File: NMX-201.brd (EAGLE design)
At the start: 50.8 x 50.2 mm, 61 parts, among them IC1 A4983TOP, IC2 A4983TOP, IC3 A4983TOP, J1 MOLEX-4-RA, J2 MOLEX-4-RA, J3 MOLEX-4-RA, U1 CADJ, U2 CADJ, U3 MOUNT-HOLE3.2, U4 MOUNT-HOLE3.2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

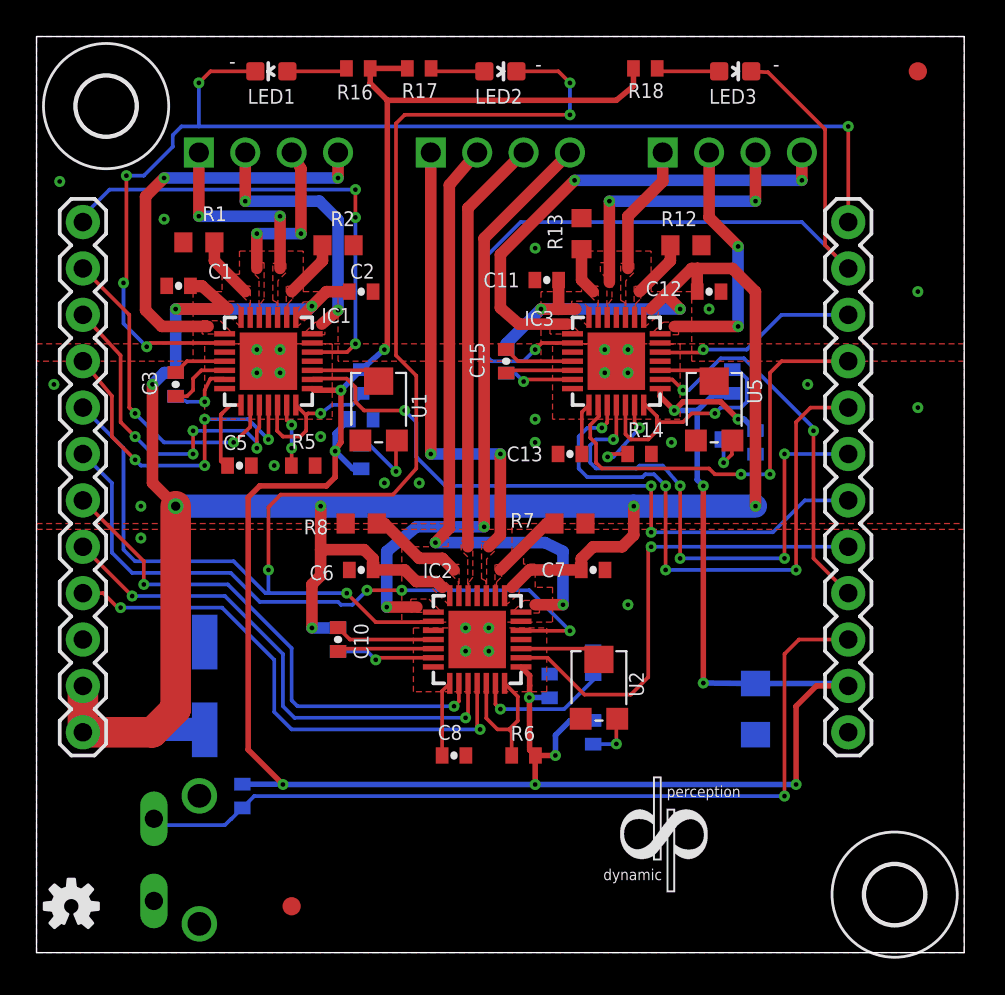
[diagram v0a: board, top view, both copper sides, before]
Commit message: Update to Silk Screen
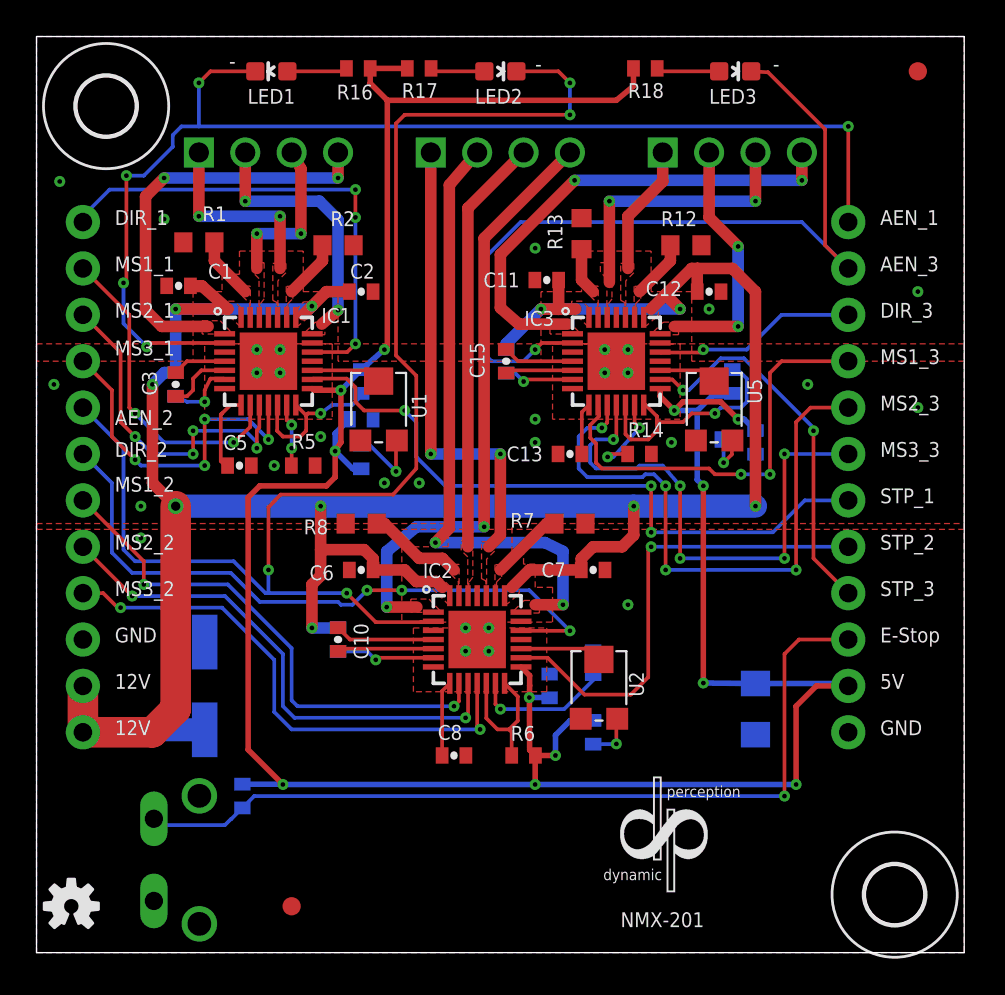
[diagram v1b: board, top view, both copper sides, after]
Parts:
- flipped JP3 to the bottom
- flipped JP4 to the bottom

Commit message: Updated NMX-201 to match NMX-201B
The only difference between NMX-201 and NMX-201B is whether the the
component attached to the motor connector ports is a screw terminal or a
Molex connector, so there's really no need to maintain two different
schematics / board files. These differences should be reflected in the
BOM instead.
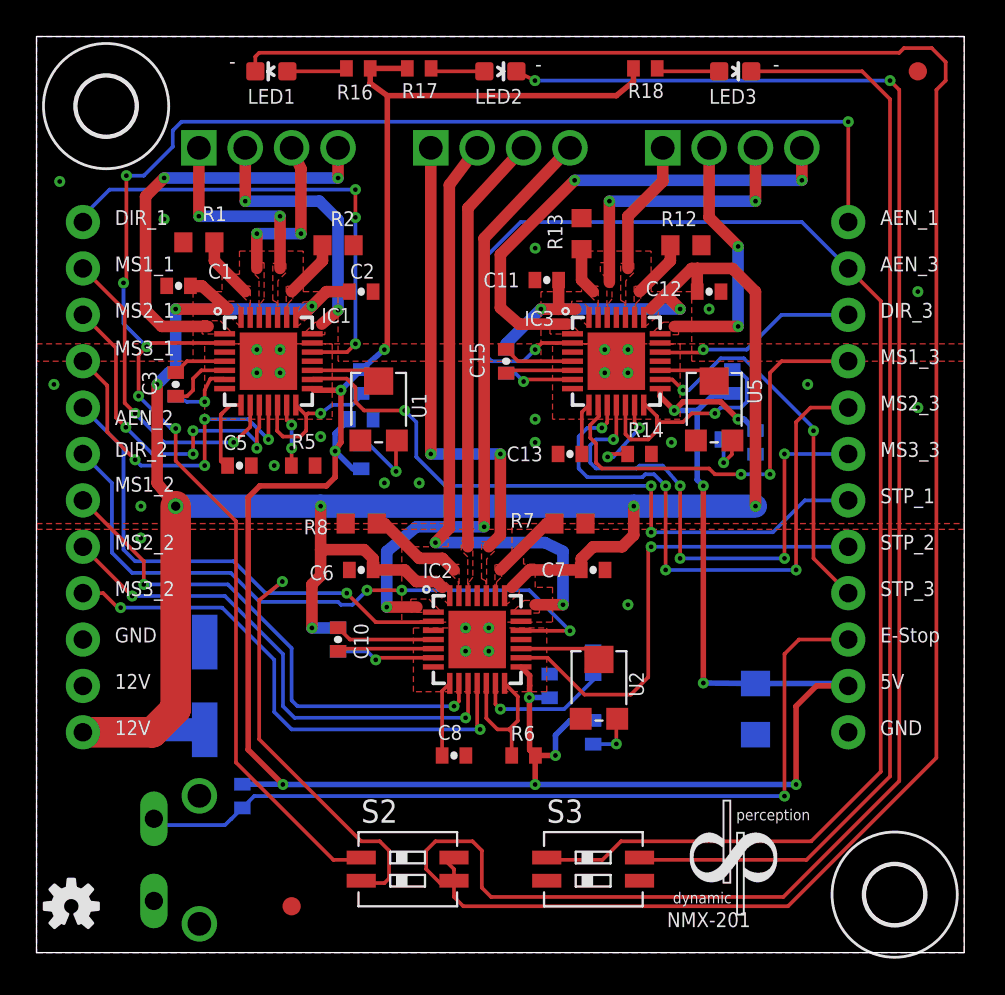
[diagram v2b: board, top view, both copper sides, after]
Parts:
- added S2, S3: CHS-02A, switch-copal:CHS-02A
- J1, J2, J3: value MOLEX-4-RA -> MOLEX-4-RAPRO-CONNECTOR; device QS_Components:MOLEX-4-RA -> NMX_StepperSide_V1-2:PRO_CONNECTOR
- R16, R17, R18: value 430 -> 14k
- moved U$1 4.02 mm to (38.1, 5.08)
- moved FRAME2 2.54 mm to (34.5, 1.40)
- moved J1 0.25 mm to (12.7, 44.1)
- moved J2 0.25 mm to (25.4, 44.1)
- moved J3 0.25 mm to (38.1, 44.1)
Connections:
- new net N$16: LED1.C, S2.4
- new net N$18: LED2.C, S2.3
- new net N$19: LED3.C, S3.4
- net AEN_1: now also S2.1; no longer LED1.C
- net AEN_2: now also S2.2; no longer LED2.C
- net AEN_3: now also S3.1; no longer LED3.C
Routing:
- net N$16: track 0.00 -> 110.2 mm
- net N$18: track 0.00 -> 93.2 mm, vias 0 -> 2
- net N$19: track 0.00 -> 61.0 mm
- net AEN_3: track 45.9 -> 81.0 mm
- net AEN_1: track 66.3 -> 95.5 mm, vias 5 -> 6
- net AEN_2: track 75.1 -> 50.7 mm, vias 4 -> 2
- net 12V: track 147.4 -> 144.4 mm
